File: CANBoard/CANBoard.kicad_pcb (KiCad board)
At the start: 4 copper layers, 40 x 40 mm, 84 parts, among them J1 Conn_01x08, J2 Conn_01x08, J3 Conn_01x08, J4 Conn_01x08, J5 SWD_10, J6 Conn_01x02, Q1 DMN2004WK, Q2 DMN2004WK, Q3 DMN2004WK, Q4 DMN2004WK, U1 MCP2551, U2 STM32F303K8Tx, U3 MB85RC256V, U4 TPS56339DDCR, U5 LD1117S33CTR, Y1 8mHz

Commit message: Swapped MCP2551 to MCP2562
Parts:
- U1: value MCP2551 -> MCP2562-H-SN

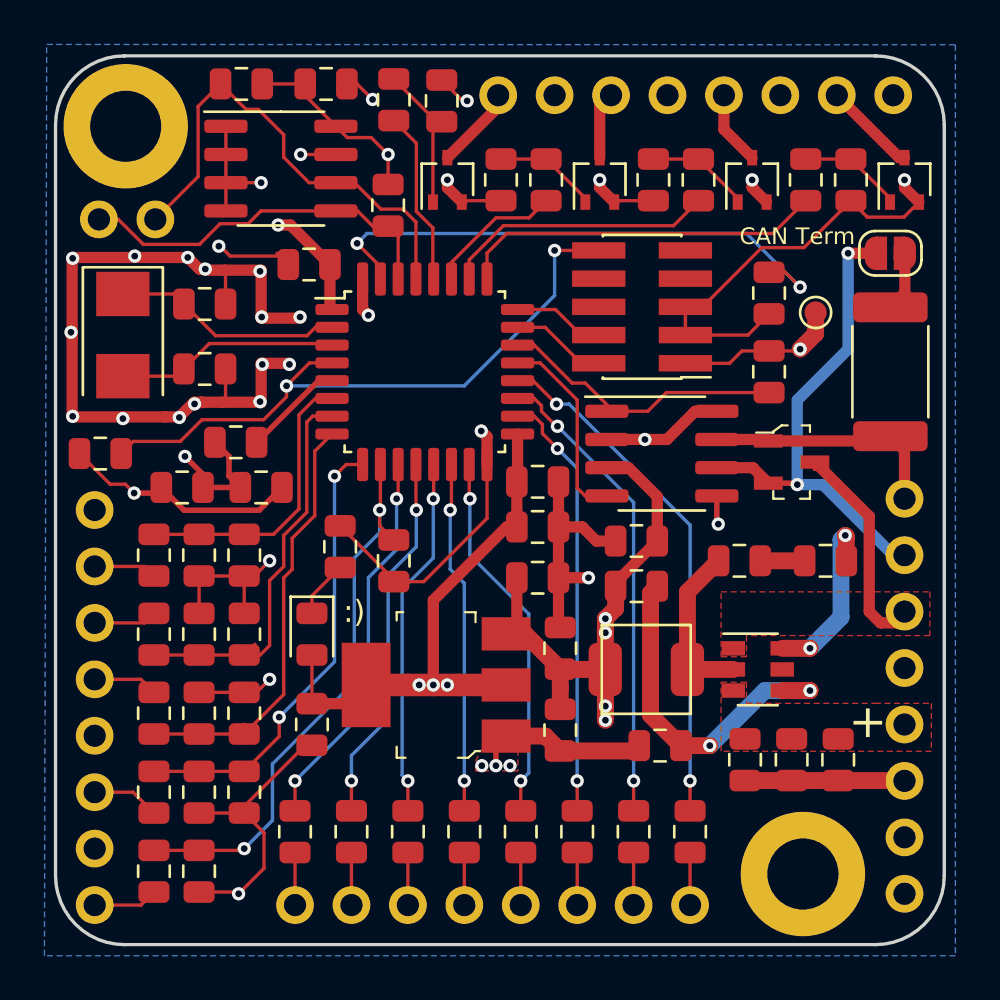
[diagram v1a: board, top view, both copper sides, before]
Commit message: Convert to kicad v6
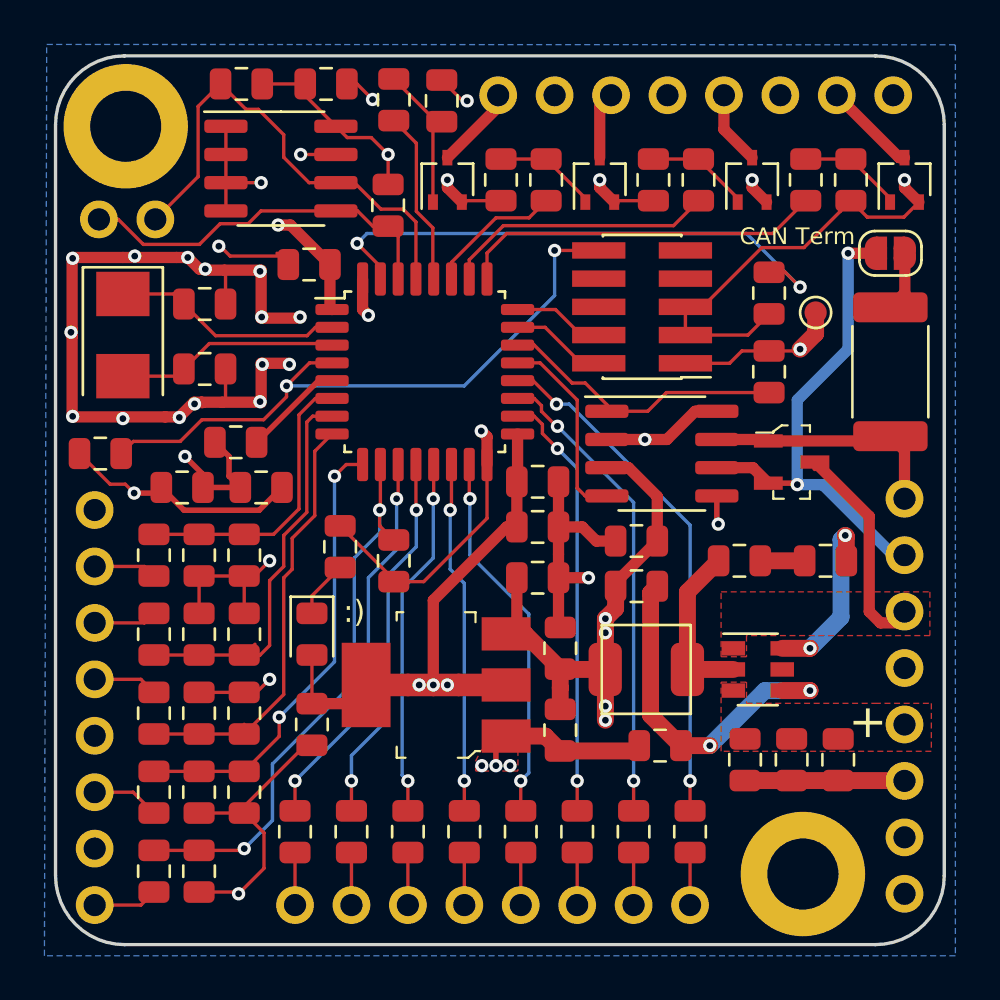
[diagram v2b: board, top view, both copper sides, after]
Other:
- net class Default removed

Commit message: V2 updates
Removed FRAM, I2C and SWD pins. Added ID solder jumpers and Tag Connect
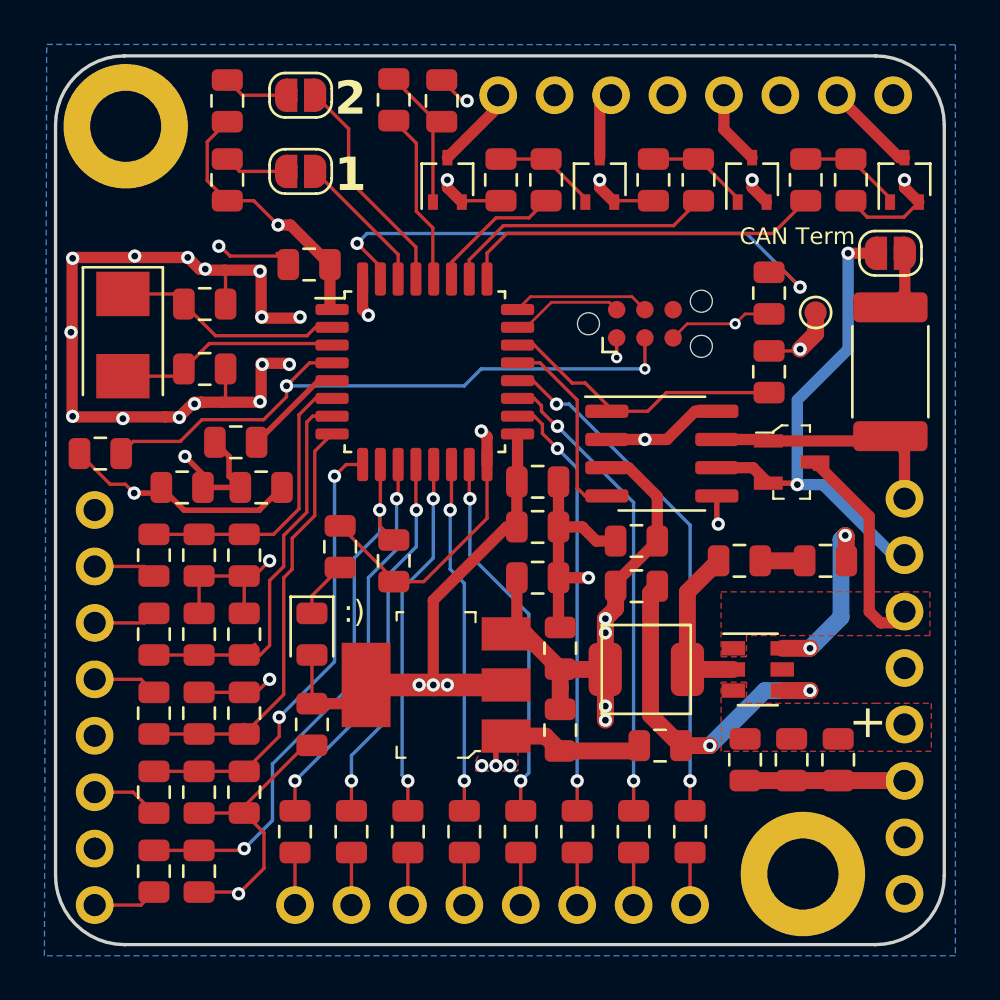
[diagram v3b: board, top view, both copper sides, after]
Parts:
- removed the C12 at (130.2, 64.3)
- removed J6: Conn_01x02, Connector_PinHeader_2.54mm:PinHeader_1x02_P2.54mm_Vertical
- removed the U3 at (128.1, 68.1)
- added JP1: CAN_ID, Jumper:SolderJumper-2_P1.3mm_Open_RoundedPad1.0x1.5mm, F.Cu at (129.0, 68.2)
- added JP2: CAN_ID, Jumper:SolderJumper-2_P1.3mm_Open_RoundedPad1.0x1.5mm, F.Cu at (129.0, 64.8)
- J5: value SWD_10 -> TC2030; footprint Connector_PinHeader_1.27mm:PinHeader_2x05_P1.27mm_Vertical_SMD -> Connector:Tag-Connect_TC2030-IDC-NL_2x03_P1.27mm_Vertical
- U3: renamed from U1; value MCP2562-H-SN -> MCP2562
- U4: renamed from U2; value STM32F303K8Tx -> STM32F303K8T6
- moved R25 8.63 mm to (125.7, 65.0), turned to -90 degrees
- moved R24 4.36 mm to (125.7, 68.6), turned to -90 degrees
- moved G1 1.66 mm to (128.3, 72.7)
- moved J5 0.77 mm to (144.5, 75.1), turned to 0 degrees
- renumbered C7 to C1, C14 to C10, C15 to C11, C16 to C12, C17 to C13, C1 to C14, C2 to C15, C3 to C16, C4 to C17, C5 to C18, C6 to C19, C8 to C2, C9 to C20, C10 to C21, C11 to C22, C18 to C3, C19 to C4, C20 to C5, C21 to C6, C22 to C7, C23 to C8, C13 to C9, D2 to D1, D1 to D2, JP1 to JP3, R30 to R1, R17 to R10, R18 to R11, R19 to R12, R20 to R13, R21 to R14, R22 to R15, R23 to R16, R24 to R17, R25 to R18, R26 to R19, R31 to R2, R27 to R20, R28 to R21, R29 to R22, R1 to R23, R34 to R24, R33 to R25, R2 to R26, R3 to R27, R4 to R28, R5 to R29, R32 to R3, R6 to R30, R7 to R31, R8 to R32, R9 to R33, R10 to R34, R11 to R35, R35 to R4, R12 to R5, R13 to R6, R14 to R7, R15 to R8, R16 to R9, U4 to U1, U5 to U2
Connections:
- J5 pad 3: GND -> /MCU/NRST
- J5 pad 6: Net-(J5-Pad6) -> unconnected-(J5-Pad6)
- R24 pad 1: /MCU/I2C_SCL -> Net-(JP1-Pad1)
- R25 pad 1: /MCU/I2C_SDA -> Net-(JP2-Pad1)
- U1 pad 5: Net-(U4-Pad5) -> unconnected-(U1-Pad5)
- U4 pad 29: /MCU/I2C_SCL -> Net-(JP2-Pad2)
- U4 pad 30: /MCU/I2C_SDA -> Net-(JP1-Pad2)
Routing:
- net /MCU/I2C_SCL: track 23.3 -> 0.00 mm
- net GND: track 166.2 -> 147.7 mm, vias 35 -> 33
- net /MCU/I2C_SDA: track 17.0 -> 0.00 mm
- net Net-(JP2-Pad2): track 0.00 -> 10.2 mm
- net Net-(JP1-Pad2): track 0.00 -> 6.39 mm
- net +3V3: track 52.8 -> 48.1 mm
- net Net-(JP2-Pad1): track 0.00 -> 2.94 mm
- net Net-(JP1-Pad1): track 0.00 -> 2.88 mm
- net /MCU/SWCLK: track 4.13 -> 6.21 mm
- net /MCU/SWDIO: track 4.32 -> 5.06 mm
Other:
- board text added: "0 0 0x640 1 0 0x641 0 1 0x642 1 1 0x643"
- board text added: "1"
- board text added: "1 2 ID"
- board text added: "2"
- board text added: "CANBoard v2"
- board text added: "CANH CANL GND GND 12V GND"
- board text added: "DI - Switch to GND only DO - Low side (0.5A Max) AI - 5V max"
- board text removed: "CANBoard v1"
- board text removed: "CANH CANL GND GND 12VSW GND"
- board text removed: "DI - Switch to GND only (No voltage) DO - Low Side Switch (0.5A Max Total) AI - 5V input max"
- board text removed: "SDA SCL"

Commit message: Updated outputs, added JLCPCB LCSC part nums
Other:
- board text added: "github.com/corygrant"
